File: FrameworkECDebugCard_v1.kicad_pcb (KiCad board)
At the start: 2 copper layers, 23.8 x 28 mm, 30 parts, among them J1 Conn_01x05, P1 1054440011, P2 2169900001, U1 FT230XS

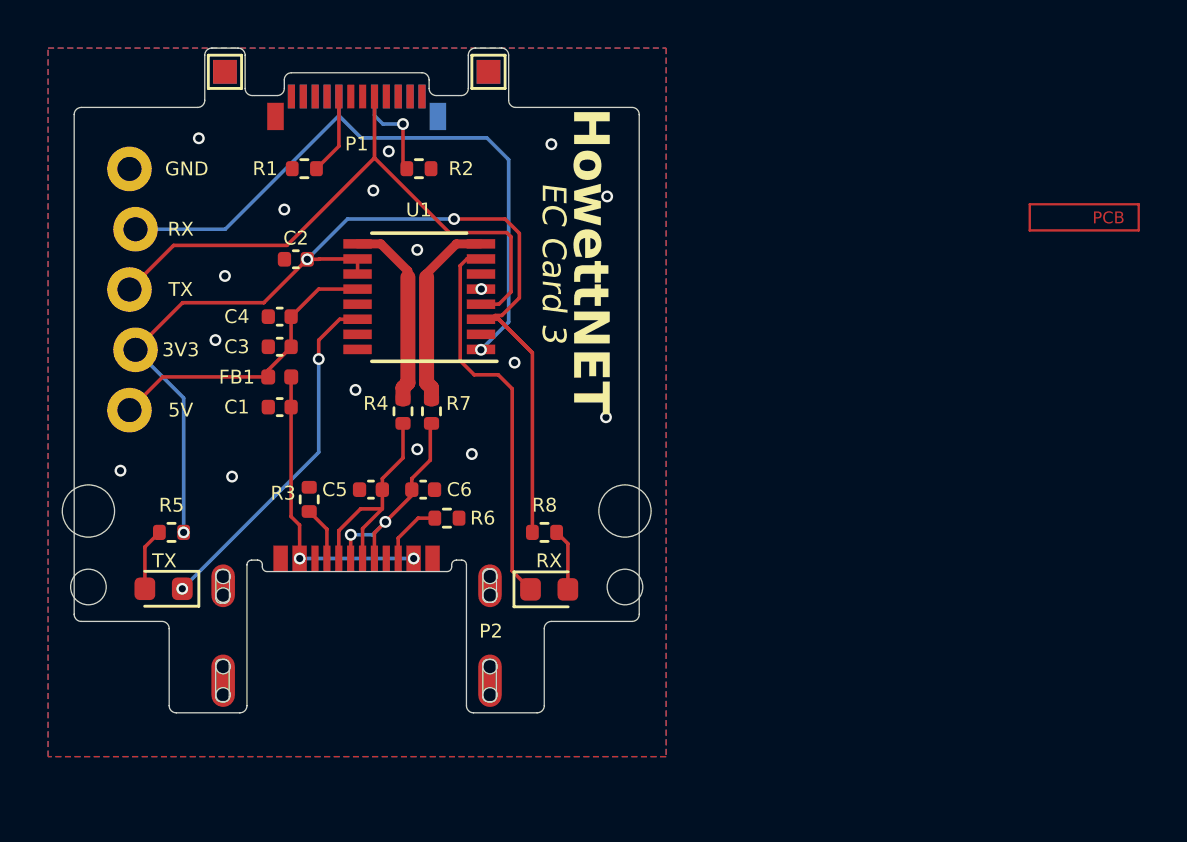
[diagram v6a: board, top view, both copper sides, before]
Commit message: ec3: length-match the D+/- pair, move logo
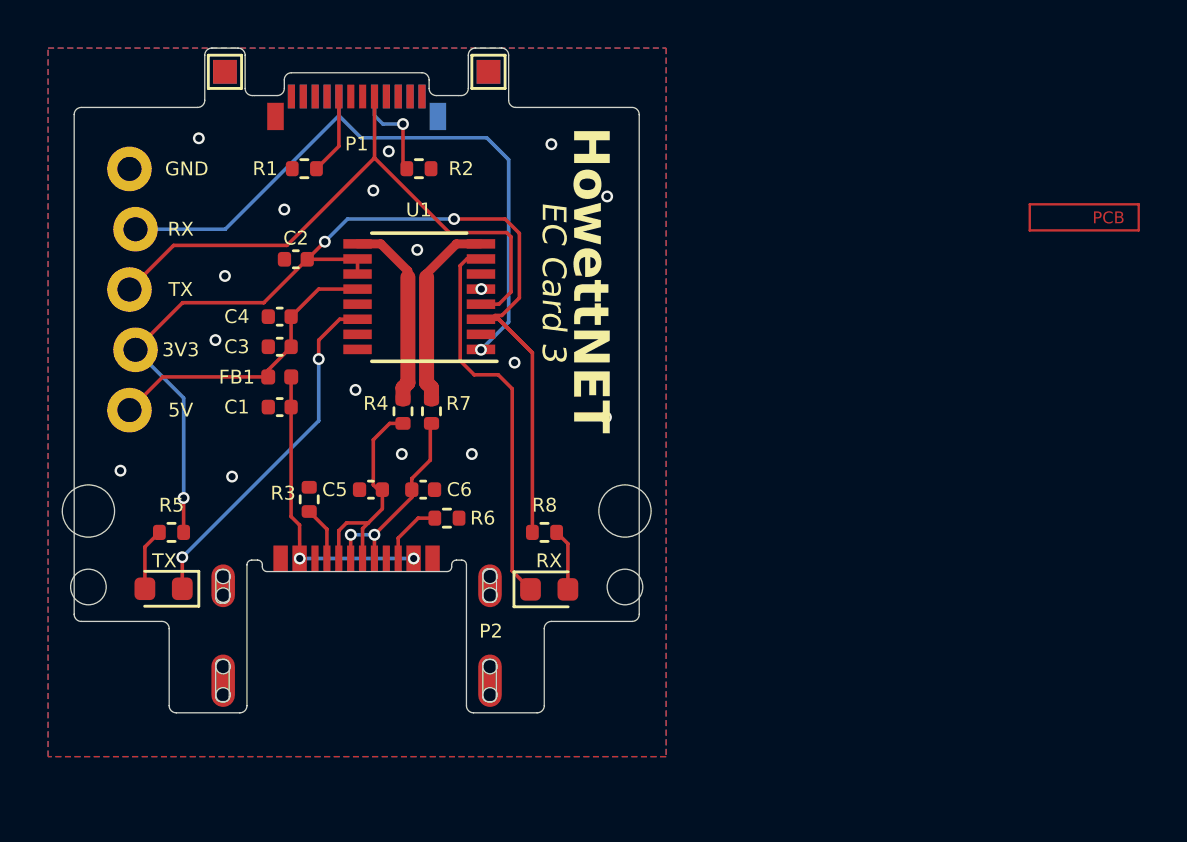
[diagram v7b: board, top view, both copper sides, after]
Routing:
- net /USBD+: track 9.37 -> 8.68 mm

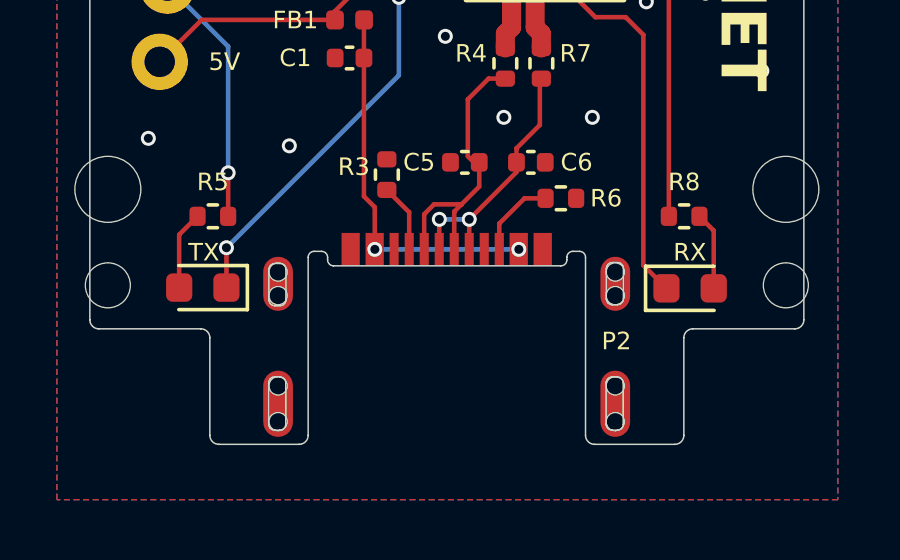
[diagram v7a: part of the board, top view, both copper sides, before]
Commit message: ec3: switch to 'real' molex footprint
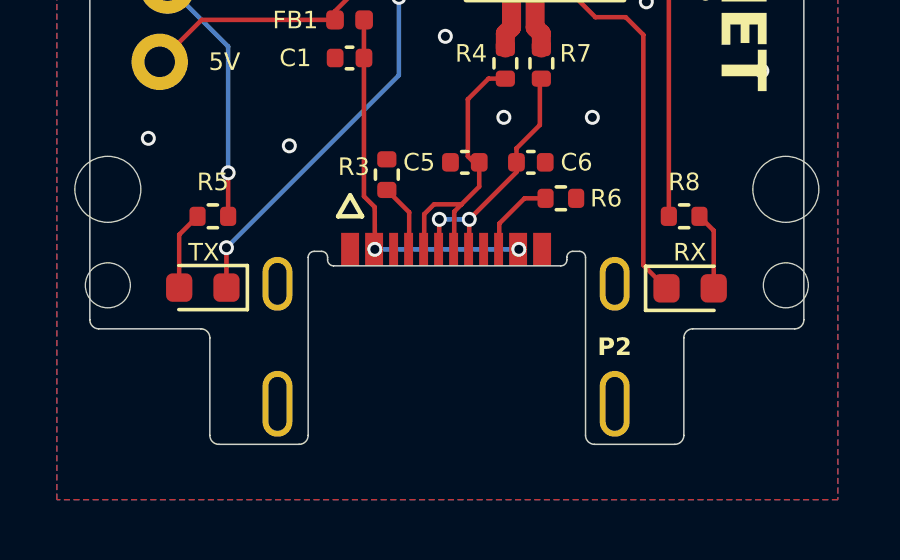
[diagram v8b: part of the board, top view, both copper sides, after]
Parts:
- P2: footprint FrameworkECDebugCard_v1:USB4510-03-1-A_GCT -> FrameworkECDebugCard_v1:MOLEX_2169900001
- moved P2 3.25 mm to (140.0, 155.8)
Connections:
- P2 pad A1: GND -> (no net)
- P2 pad A4: Net-(C1-Pad1) -> (no net)
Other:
- outline, holes or cut-outs redrawn
